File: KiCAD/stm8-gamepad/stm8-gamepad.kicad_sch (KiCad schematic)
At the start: 28 parts, among them J1 batt., J2 batt., J3 SWIM con., J4 speaker, J5 speaker, J6 video out, SW1 power, SW2 LEFT, SW3 UP, SW4 DOWN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

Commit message: Version NUCLEO-8S207K8 créé
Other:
- added sheet nucleo-8s207k8 (nucleo-8s207k8.kicad_sch)
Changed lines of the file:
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@@
     (pin "2")
+  )
+  (sheet (at 266.065 15.24) (size 18.415 18.415) (fields_autoplaced)
+    (stroke (width 0.1524) (type solid) (color 0 0 0 0))
+    (fill (color 0 0 0 0.0000))
+    (property "Sheet name" "nucleo-8s207k8" (id 0) (at 266.065 14.5284 0)
+      (effects (font (size 1.27 1.27)) (justify left bottom))
+    )
+    (property "Sheet file" "nucleo-8s207k8.kicad_sch" (id 1) (at 266.065 34.2396 0)
+      (effects (font (size 1.27 1.27)) (justify left top))
+    )
   )
   (sheet_instances
     (path "/" (page "1"))
+    (path "/3f423e78-9a93-4158-a149-1324034fba40" (page "2"))
   )
   (symbol_instances
@@
       (reference "#PWR010") (unit 1) (value "GND") (footprint "")
     )
+    (path "/3f423e78-9a93-4158-a149-1324034fba40/432dda3e-c41b-4fe1-93a0-a25899b27731"
+      (reference "#PWR011") (unit 1) (value "GND") (footprint "")
+    )
+    (path "/3f423e78-9a93-4158-a149-1324034fba40/1f22284f-661c-4a5f-84ee-0cfaf595c8b2"
+      (reference "#PWR012") (unit 1) (value "GND") (footprint "")
+    )
+    (path "/3f423e78-9a93-4158-a149-1324034fba40/ab370fce-260d-441e-8cfa-9fd31e9076c0"
+      (reference "#PWR013") (unit 1) (value "GND") (footprint "")
+    )
+    (path "/3f423e78-9a93-4158-a149-1324034fba40/f845f27f-445e-4244-8807-ac524f4c8299"
+      (reference "#PWR014") (unit 1) (value "GND") (footprint "")
+    )
+    (path "/3f423e78-9a93-4158-a149-1324034fba40/b65b3566-3b8d-4121-afa1-5b404bf50161"
+      (reference "#PWR015") (unit 1) (value "GND") (footprint "")
+    )
+    (path "/3f423e78-9a93-4158-a149-1324034fba40/7692f75f-dfa5-48b8-bb56-d412d084e638"
+      (reference "#PWR016") (unit 1) (value "GND") (footprint "")
+    )
+    (path "/3f423e78-9a93-4158-a149-1324034fba40/7a3d71a6-f149-42f4-9e34-fe0b02fc839d"
+      (reference "#PWR017") (unit 1) (value "GND") (footprint "")
+    )
     (path "/2b1531aa-aa31-417e-a951-4a28ff0dcd74"
       (reference "3VDC1") (unit 1) (value "2xAA") (footprint "")
     )
+    (path "/3f423e78-9a93-4158-a149-1324034fba40/bde456a9-9867-45cc-9ddd-fdd6ce4556b9"
+      (reference "3VDC2") (unit 1) (value "2xAA") (footprint "")
+    )
     (path "/07ed504c-5c88-44c6-8ff9-c32de70e566a"
       (reference "C1") (unit 1) (value "100nF") (footprint "")
@@
       (reference "C6") (unit 1) (value "10µF") (footprint "")
     )
+    (path "/3f423e78-9a93-4158-a149-1324034fba40/368021b5-358e-48ea-b079-22e09d35f767"
+      (reference "C7") (unit 1) (value "18pF") (footprint "")
+    )
+    (path "/3f423e78-9a93-4158-a149-1324034fba40/b875562c-ac50-44c4-a154-a8be80bdd72c"
+      (reference "C8") (unit 1) (value "18pF") (footprint "")
+    )
+    (path "/3f423e78-9a93-4158-a149-1324034fba40/f7bbd77a-18f5-46b5-aaf9-34799637ac2b"
+      (reference "C9") (unit 1) (value "10µF") (footprint "")
+    )
     (path "/4a228d23-5adc-4ec7-9422-0a63c57cd8a6"
       (reference "D1") (unit 1) (value "1N4148") (footprint "Diode_THT:D_DO-35_SOD27_P7.62mm_Horizontal")
@@
       (reference "J6") (unit 1) (value "video out") (footprint "")
     )
+    (path "/3f423e78-9a93-4158-a149-1324034fba40/e8c6bfec-7395-49f6-810b-1d8527105637"
+      (reference "J7") (unit 1) (value "batt.") (footprint "")
+    )
+    (path "/3f423e78-9a93-4158-a149-1324034fba40/ad1ebe3b-d770-4aa4-8ba2-64c24f92e640"
+      (reference "J8") (unit 1) (value "batt.") (footprint "")
+    )
+    (path "/3f423e78-9a93-4158-a149-1324034fba40/05f79583-924a-413b-9514-a6ac2a520b1c"
+      (reference "J9") (unit 1) (value "audio out") (footprint "")
+    )
+    (path "/3f423e78-9a93-4158-a149-1324034fba40/96f0c13d-b6bd-414d-867c-5c8a6fed7aeb"
+      (reference "J10") (unit 1) (value "video out") (footprint "")
+    )
     (path "/bcf077a1-37d1-42aa-beed-4cbc61cc439e"
       (reference "LS1") (unit 1) (value "150 ohm") (footprint "")
@@
       (reference "R4") (unit 1) (value "150") (footprint "")
     )
+    (path "/3f423e78-9a93-4158-a149-1324034fba40/bd271d0a-0fc9-4de7-9bab-bcd5b8309c19"
+      (reference "R5") (unit 1) (value "150") (footprint "")
+    )
+    (path "/3f423e78-9a93-4158-a149-1324034fba40/8c0e7c92-1019-4049-a7b9-7ecd7fce3bde"
+      (reference "R6") (unit 1) (value "270") (footprint "")
+    )
+    (path "/3f423e78-9a93-4158-a149-1324034fba40/5f5c70b0-2b4d-4f0c-8eb8-890565cee242"
+      (reference "R7") (unit 1) (value "2K") (footprint "")
+    )
+    (path "/3f423e78-9a93-4158-a149-1324034fba40/1ba2505f-21a1-407b-aeb6-8ee6e09e537e"
+      (reference "R8") (unit 1) (value "150") (footprint "")
+    )
     (path "/a4a47845-bde1-4754-82c8-ad2e7b30b918"
       (reference "SW1") (unit 1) (value "power") (footprint "")
@@
       (reference "SW7") (unit 1) (value "A") (footprint "")
     )
+    (path "/3f423e78-9a93-4158-a149-1324034fba40/365fff58-9467-4d33-be30-4978f4c7d3f8"
+      (reference "SW8") (unit 1) (value "power") (footprint "")
+    )
+    (path "/3f423e78-9a93-4158-a149-1324034fba40/6e230596-3273-4b9e-a665-2c3936388330"
+      (reference "SW9") (unit 1) (value "LEFT") (footprint "")
+    )
+    (path "/3f423e78-9a93-4158-a149-1324034fba40/6430d890-e319-4d28-a998-c8b6b52d08fb"
+      (reference "SW10") (unit 1) (value "UP") (footprint "")
+    )
+    (path "/3f423e78-9a93-4158-a149-1324034fba40/f0a136a5-8e68-486e-b246-b8739497b727"
+      (reference "SW11") (unit 1) (value "DOWN") (footprint "")
+    )
+    (path "/3f423e78-9a93-4158-a149-1324034fba40/1b372ffb-d496-4c29-a537-3d989b6f1ce0"
+      (reference "SW12") (unit 1) (value "RIGHT") (footprint "")
+    )
+    (path "/3f423e78-9a93-4158-a149-1324034fba40/091d9253-ae3b-4d22-a0fe-2bce76e55536"
+      (reference "SW13") (unit 1) (value "B") (footprint "")
+    )
+    (path "/3f423e78-9a93-4158-a149-1324034fba40/1ea4e3ca-efc9-4c75-b72e-65404c6f7d29"
+      (reference "SW14") (unit 1) (value "A") (footprint "")
+    )
     (path "/8be3051d-675b-4759-a665-6256a3edee23"
       (reference "U1") (unit 1) (value "STM8S207K8T6") (footprint "")
@@
       (reference "Y1") (unit 1) (value "16Mhz") (footprint "")
     )
-  )
+    (path "/3f423e78-9a93-4158-a149-1324034fba40/9495883e-4eeb-49b6-8648-2df4d6aa01d1"
+      (reference "Y2") (unit 1) (value "16Mhz") (footprint "")
+    )
+  )

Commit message: modification prototype 1
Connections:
- net BTN_A: now also U1.11 (AIN5/PB5); no longer U1.27 (T3_CH1/PD2)
- net BTN_B: now also U1.12 (AIN4/PB4); no longer U1.28 (T2_CH2/PD3)
- net DOWN: now also U1.15 (AIN1/PB1); no longer U1.31 (UART3RX/PD6)
- net LEFT: now also U1.16 (AIN0/PB0); no longer U1.29 (T2_CH1/PD4)
- net RIGHT: now also U1.14 (AIN2/PB2); no longer U1.30 (UART3TX/PD5)
- net UP: now also U1.13 (AIN3/PB3); no longer U1.32 (TLI/PD7)
- no-connect marks 0 -> 13
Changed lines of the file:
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@@
   (junction (at 132.08 112.395) (diameter 0) (color 0 0 0 0)
   )
+  (junction (at 135.89 112.395) (diameter 0) (color 0 0 0 0)
+  )
   (junction (at 135.89 102.235) (diameter 0) (color 0 0 0 0)
   )
@@
   (junction (at 125.095 35.56) (diameter 0) (color 0 0 0 0)
   )
-  (junction (at 135.89 112.395) (diameter 0) (color 0 0 0 0)
-  )
   (junction (at 97.155 86.995) (diameter 0) (color 0 0 0 0)
   )
+  (no_connect (at 174.625 86.995))
+  (no_connect (at 174.625 107.315))
+  (no_connect (at 174.625 89.535))
+  (no_connect (at 174.625 94.615))
+  (no_connect (at 174.625 114.935))
+  (no_connect (at 174.625 120.015))
+  (no_connect (at 174.625 84.455))
+  (no_connect (at 147.955 99.695))
+  (no_connect (at 174.625 102.235))
+  (no_connect (at 174.625 109.855))
+  (no_connect (at 174.625 117.475))
+  (no_connect (at 174.625 92.075))
+  (no_connect (at 174.625 81.915))
   (wire (pts (xy 123.825 94.615) (xy 127.635 94.615))
     (stroke (width 0) (type default) (color 0 0 0 0))
@@
     (stroke (width 0) (type default) (color 0 0 0 0))
   )
-  (wire (pts (xy 174.625 92.075) (xy 176.53 92.075))
-    (stroke (width 0) (type default) (color 0 0 0 0))
-  )
   (wire (pts (xy 138.43 50.8) (xy 160.02 50.8))
     (stroke (width 0) (type default) (color 0 0 0 0))
@@
     (stroke (width 0) (type default) (color 0 0 0 0))
   )
-  (wire (pts (xy 174.625 89.535) (xy 176.53 89.535))
-    (stroke (width 0) (type default) (color 0 0 0 0))
-  )
   (wire (pts (xy 132.715 95.885) (xy 142.875 95.885))
     (stroke (width 0) (type default) (color 0 0 0 0))
@@
     (stroke (width 0) (type default) (color 0 0 0 0))
   )
+  (wire (pts (xy 139.065 104.775) (xy 139.065 112.395))
+    (stroke (width 0) (type default) (color 0 0 0 0))
+  )
   (wire (pts (xy 138.43 59.055) (xy 138.43 50.8))
     (stroke (width 0) (type default) (color 0 0 0 0))
@@
     (stroke (width 0) (type default) (color 0 0 0 0))
   )
-  (wire (pts (xy 141.605 104.775) (xy 141.605 112.395))
-    (stroke (width 0) (type default) (color 0 0 0 0))
-  )
   (wire (pts (xy 174.625 99.695) (xy 199.39 99.695))
     (stroke (width 0) (type default) (color 0 0 0 0))
@@
     (stroke (width 0) (type default) (color 0 0 0 0))
   )
-  (wire (pts (xy 147.955 104.775) (xy 141.605 104.775))
+  (wire (pts (xy 139.065 104.775) (xy 147.955 104.775))
     (stroke (width 0) (type default) (color 0 0 0 0))
   )
@@
     (stroke (width 0) (type default) (color 0 0 0 0))
   )
-  (wire (pts (xy 174.625 81.915) (xy 176.53 81.915))
-    (stroke (width 0) (type default) (color 0 0 0 0))
-  )
   (wire (pts (xy 114.935 44.45) (xy 126.365 44.45))
     (stroke (width 0) (type default) (color 0 0 0 0))
@@
     (stroke (width 0) (type default) (color 0 0 0 0))
   )
-  (wire (pts (xy 174.625 84.455) (xy 176.53 84.455))
-    (stroke (width 0) (type default) (color 0 0 0 0))
-  )
   (wire (pts (xy 114.935 35.56) (xy 114.935 44.45))
     (stroke (width 0) (type default) (color 0 0 0 0))
   )
-  (wire (pts (xy 174.625 94.615) (xy 176.53 94.615))
-    (stroke (width 0) (type default) (color 0 0 0 0))
-  )
   (wire (pts (xy 112.395 46.99) (xy 114.935 46.99))
     (stroke (width 0) (type default) (color 0 0 0 0))
@@
     (stroke (width 0) (type default) (color 0 0 0 0))
   )
-  (wire (pts (xy 174.625 86.995) (xy 176.53 86.995))
-    (stroke (width 0) (type default) (color 0 0 0 0))
-  )
   (wire (pts (xy 144.145 99.695) (xy 144.145 97.155))
     (stroke (width 0) (type default) (color 0 0 0 0))
@@
     (stroke (width 0) (type default) (color 0 0 0 0))
   )
+  (wire (pts (xy 139.065 112.395) (xy 135.89 112.395))
+    (stroke (width 0) (type default) (color 0 0 0 0))
+  )
   (wire (pts (xy 113.665 45.72) (xy 113.665 27.305))
     (stroke (width 0) (type default) (color 0 0 0 0))
@@
     (stroke (width 0) (type default) (color 0 0 0 0))
   )
-  (wire (pts (xy 135.89 112.395) (xy 141.605 112.395))
-    (stroke (width 0) (type default) (color 0 0 0 0))
-  )
   (wire (pts (xy 142.875 95.885) (xy 142.875 92.075))
     (stroke (width 0) (type default) (color 0 0 0 0))
@@
     (stroke (width 0) (type default) (color 0 0 0 0))
   )
-  (global_label "BTN_B" (shape input) (at 176.53 92.075 0) (fields_autoplaced)
-    (effects (font (size 1 1)) (justify left))
-    (property "Références Inter-Feuilles" "${INTERSHEET_REFS}" (id 0) (at 183.0014 92.0125 0)
-      (effects (font (size 1 1)) (justify left) hide)
-    )
-  )
-  (global_label "RIGHT" (shape input) (at 176.53 86.995 0) (fields_autoplaced)
-    (effects (font (size 1 1)) (justify left))
-    (property "Références Inter-Feuilles" "${INTERSHEET_REFS}" (id 0) (at 182.7157 86.9325 0)
-      (effects (font (size 1 1)) (justify left) hide)
+  (global_label "BTN_B" (shape input) (at 147.955 109.855 180) (fields_autoplaced)
+    (effects (font (size 1 1)) (justify right))
+    (property "Références Inter-Feuilles" "${INTERSHEET_REFS}" (id 0) (at 141.4836 109.9175 0)
+      (effects (font (size 1 1)) (justify right) hide)
+    )
+  )
+  (global_label "RIGHT" (shape input) (at 147.955 114.935 180) (fields_autoplaced)
+    (effects (font (size 1 1)) (justify right))
+    (property "Références Inter-Feuilles" "${INTERSHEET_REFS}" (id 0) (at 141.7693 114.9975 0)
+      (effects (font (size 1 1)) (justify right) hide)
     )
   )
@@
     )
   )
-  (global_label "LEFT" (shape input) (at 176.53 89.535 0) (fields_autoplaced)
-    (effects (font (size 1 1)) (justify left))
-    (property "Références Inter-Feuilles" "${INTERSHEET_REFS}" (id 0) (at 181.7633 89.5975 0)
-      (effects (font (size 1 1)) (justify left) hide)
+  (global_label "LEFT" (shape input) (at 147.955 120.015 180) (fields_autoplaced)
+    (effects (font (size 1 1)) (justify right))
+    (property "Références Inter-Feuilles" "${INTERSHEET_REFS}" (id 0) (at 142.7217 119.9525 0)
+      (effects (font (size 1 1)) (justify right) hide)
     )
   )
@@
     )
   )
-  (global_label "DOWN" (shape input) (at 176.53 84.455 0) (fields_autoplaced)
-    (effects (font (size 1 1)) (justify left))
-    (property "Références Inter-Feuilles" "${INTERSHEET_REFS}" (id 0) (at 182.6681 84.5175 0)
-      (effects (font (size 1 1)) (justify left) hide)
+  (global_label "DOWN" (shape input) (at 147.955 117.475 180) (fields_autoplaced)
+    (effects (font (size 1 1)) (justify right))
+    (property "Références Inter-Feuilles" "${INTERSHEET_REFS}" (id 0) (at 141.8169 117.4125 0)
+      (effects (font (size 1 1)) (justify right) hide)
     )
   )
@@
     )
   )
-  (global_label "UP" (shape input) (at 176.53 81.915 0) (fields_autoplaced)
-    (effects (font (size 1 1)) (justify left))
-    (property "Références Inter-Feuilles" "${INTERSHEET_REFS}" (id 0) (at 180.4776 81.8525 0)
-      (effects (font (size 1 1)) (justify left) hide)
+  (global_label "UP" (shape input) (at 147.955 112.395 180) (fields_autoplaced)
+    (effects (font (size 1 1)) (justify right))
+    (property "Références Inter-Feuilles" "${INTERSHEET_REFS}" (id 0) (at 144.0074 112.4575 0)
+      (effects (font (size 1 1)) (justify right) hide)
     )
   )
@@
     )
   )
-  (global_label "BTN_A" (shape input) (at 176.53 94.615 0) (fields_autoplaced)
-    (effects (font (size 1 1)) (justify left))
-    (property "Références Inter-Feuilles" "${INTERSHEET_REFS}" (id 0) (at 182.8586 94.5525 0)
-      (effects (font (size 1 1)) (justify left) hide)
+  (global_label "BTN_A" (shape input) (at 147.955 107.315 180) (fields_autoplaced)
+    (effects (font (size 1 1)) (justify right))
+    (property "Références Inter-Feuilles" "${INTERSHEET_REFS}" (id 0) (at 141.6264 107.3775 0)
+      (effects (font (size 1 1)) (justify right) hide)
     )
   )
@@
       (effects (font (size 1.27 1.27)) (justify left))
     )
-    (property "Value" "100nF" (id 1) (at 135.89 111.125 0)
-      (effects (font (size 1.27 1.27)) (justify left))
-    )
+    (property "Value" "100nF" (id 1) (at 129.54 106.045 0)
+      (effects (font (size 1.27 1.27)) (justify left))
+    )

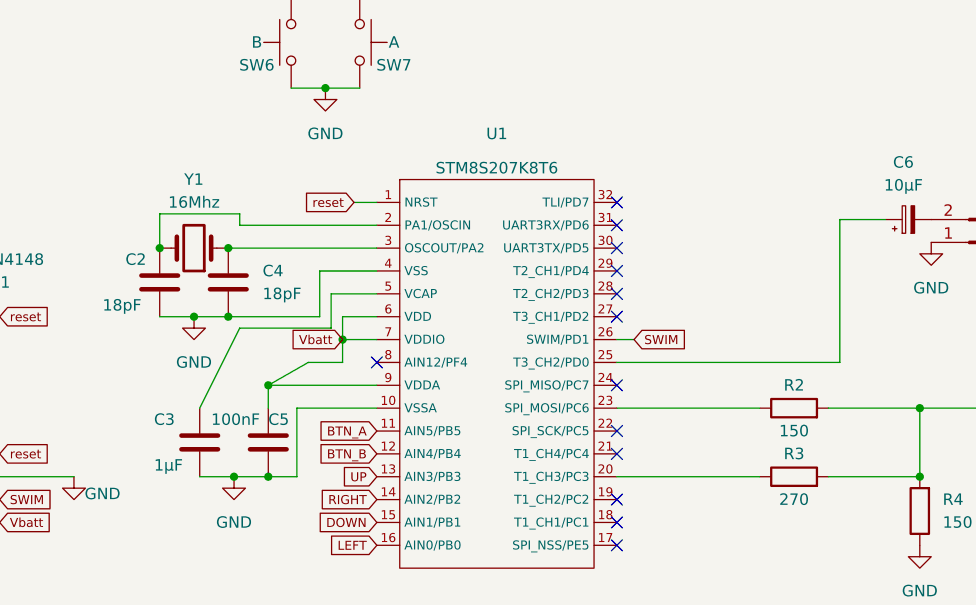
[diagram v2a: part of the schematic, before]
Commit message: Modification matérielle cristal de 16Mhz remplacé par 24Mhz. Amélioration du rapport largeur/hauteur de l'image maintenant proche de l'utnité
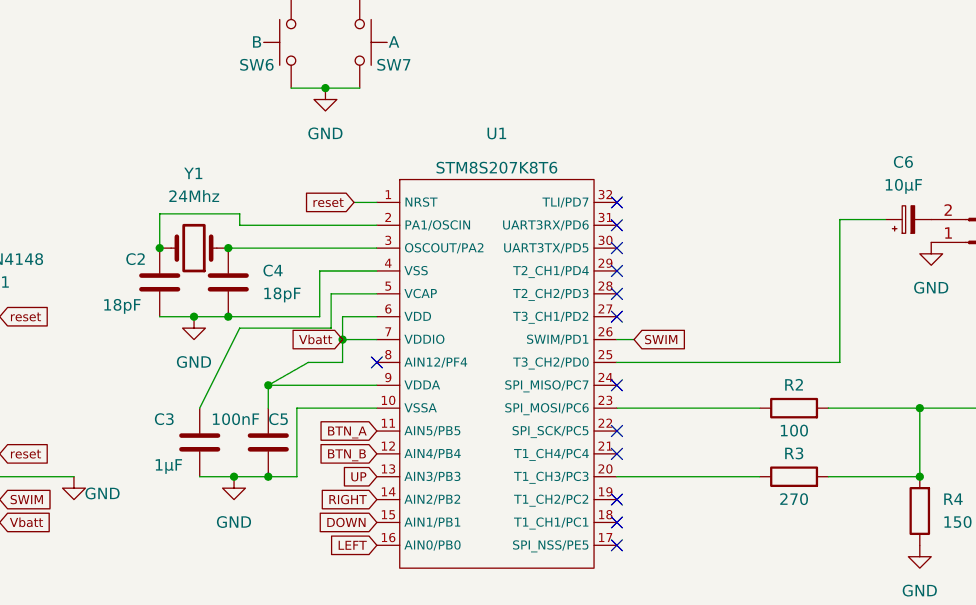
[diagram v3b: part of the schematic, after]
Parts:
- R2: value 150 -> 100
- Y1: value 16Mhz -> 24Mhz
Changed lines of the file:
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@@
   (symbol (lib_id "Device:Crystal") (at 127.635 86.995 180) (unit 1)
     (in_bom yes) (on_board yes) (fields_autoplaced)
-    (property "Reference" "Y1" (id 0) (at 127.635 79.375 0))
-    (property "Value" "16Mhz" (id 1) (at 127.635 81.915 0))
+    (property "Reference" "Y1" (id 0) (at 127.635 78.74 0))
+    (property "Value" "24Mhz" (id 1) (at 127.635 81.28 0))
     (property "Footprint" "" (id 2) (at 127.635 86.995 0)
       (effects (font (size 1.27 1.27)) hide)
@@
     (in_bom yes) (on_board yes)
     (property "Reference" "R2" (id 0) (at 194.31 102.235 90))
-    (property "Value" "150" (id 1) (at 194.31 107.315 90))
+    (property "Value" "100" (id 1) (at 194.31 107.315 90))
     (property "Footprint" "" (id 2) (at 194.31 106.553 90)
       (effects (font (size 1.27 1.27)) hide)
@@
     )
     (path "/b9ea2e14-051a-4aab-9599-98e5d45fd736"
-      (reference "R2") (unit 1) (value "150") (footprint "")
+      (reference "R2") (unit 1) (value "100") (footprint "")
     )
     (path "/ab47d6f0-bde7-4f5d-959c-98201f237641"
@@
     )
     (path "/3f423e78-9a93-4158-a149-1324034fba40/bd271d0a-0fc9-4de7-9bab-bcd5b8309c19"
-      (reference "R5") (unit 1) (value "150") (footprint "")
+      (reference "R5") (unit 1) (value "100") (footprint "")
     )
     (path "/3f423e78-9a93-4158-a149-1324034fba40/8c0e7c92-1019-4049-a7b9-7ecd7fce3bde"
@@
     )
     (path "/9bb99e72-c974-40c5-91f5-ac09e1f9fa5f"
-      (reference "Y1") (unit 1) (value "16Mhz") (footprint "")
+      (reference "Y1") (unit 1) (value "24Mhz") (footprint "")
     )
     (path "/3f423e78-9a93-4158-a149-1324034fba40/9495883e-4eeb-49b6-8648-2df4d6aa01d1"
-      (reference "Y2") (unit 1) (value "16Mhz") (footprint "")
-    )
-  )
+      (reference "Y2") (unit 1) (value "24Mhz") (footprint "")
+    )
+  )
